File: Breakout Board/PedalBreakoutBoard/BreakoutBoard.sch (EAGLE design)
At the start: 40 parts, among them U1 ES_DAISY_SEED_REV4

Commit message: DP-16 - Update schematic to add new sheet
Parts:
- added J1: POWER_JACK, SparkFun-Connectors:POWER_JACK
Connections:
- new net 9V_IN: U1.V_IN
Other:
- note added: "?????"

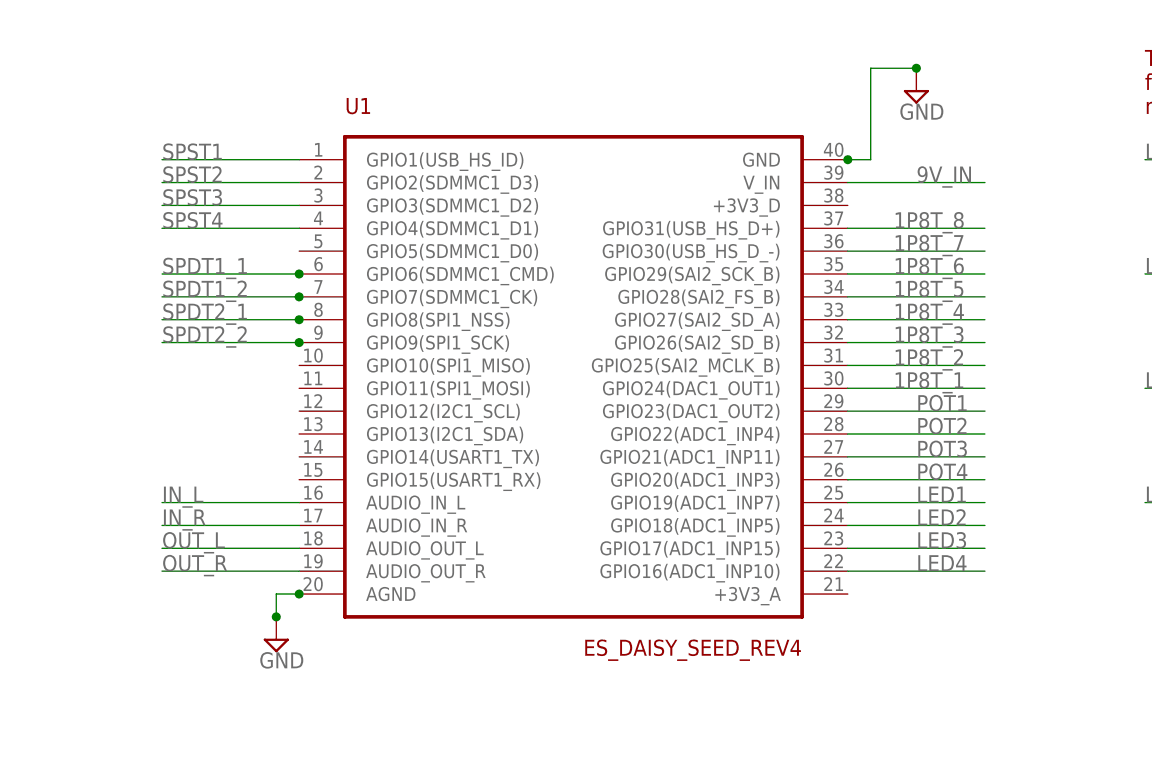
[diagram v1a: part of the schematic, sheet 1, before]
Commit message: DP-16 - Update schematic with correct 3V3 feeds
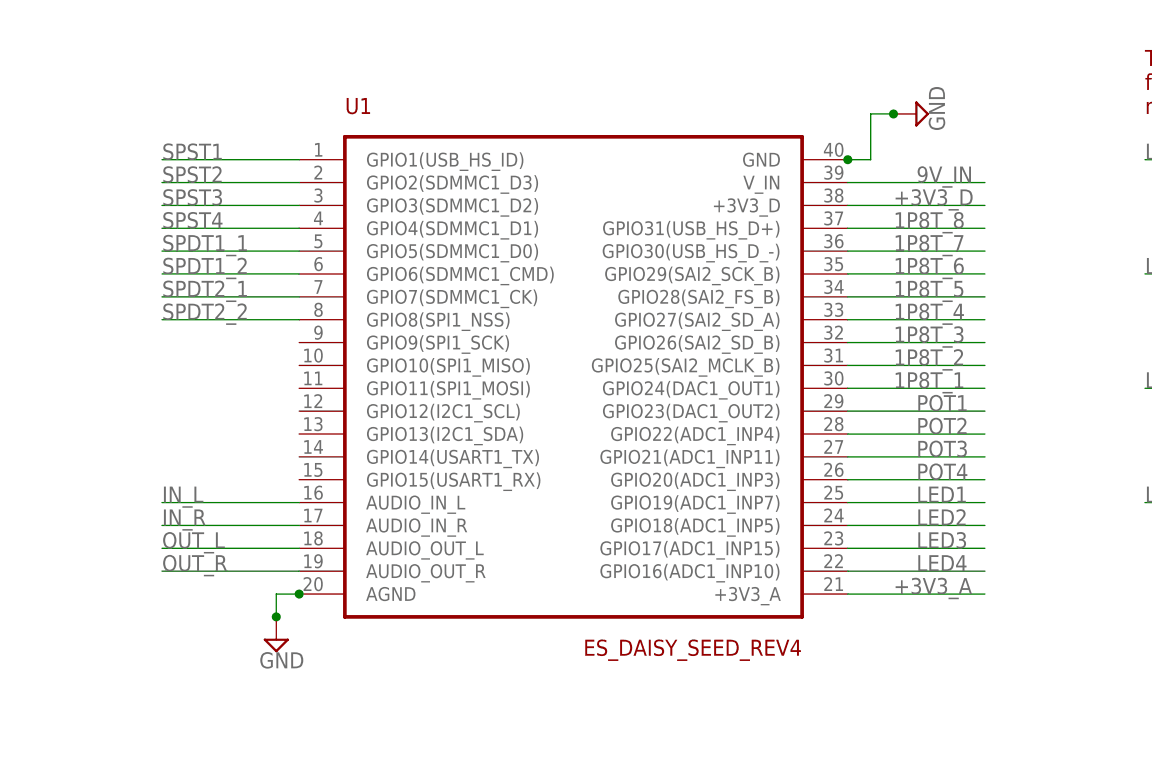
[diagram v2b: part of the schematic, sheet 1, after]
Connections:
- removed net +3V3: 1P8T.9, POT1.1, POT2.1, POT3.1, POT4.1, SPDT1.2, SPDT2.2, SPST1.1, SPST2.1, SPST3.1, SPST4.1
- new net +3V3_A: 1P8T.9, POT1.1, POT2.1, POT3.1, POT4.1, SPDT1.2, SPDT2.2, SPST1.1, SPST2.1, SPST3.1, SPST4.1, U1.+3V3_A
- new net +3V3_D: U1.+3V3_D
- net SPDT1_1: now also U1.GPIO5(SDMMC1_D0); no longer U1.GPIO6(SDMMC1_CMD)
- net SPDT1_2: now also U1.GPIO6(SDMMC1_CMD); no longer U1.GPIO7(SDMMC1_CK)
- net SPDT2_1: now also U1.GPIO7(SDMMC1_CK); no longer U1.GPIO8(SPI1_NSS)
- net SPDT2_2: now also U1.GPIO8(SPI1_NSS); no longer U1.GPIO9(SPI1_SCK)

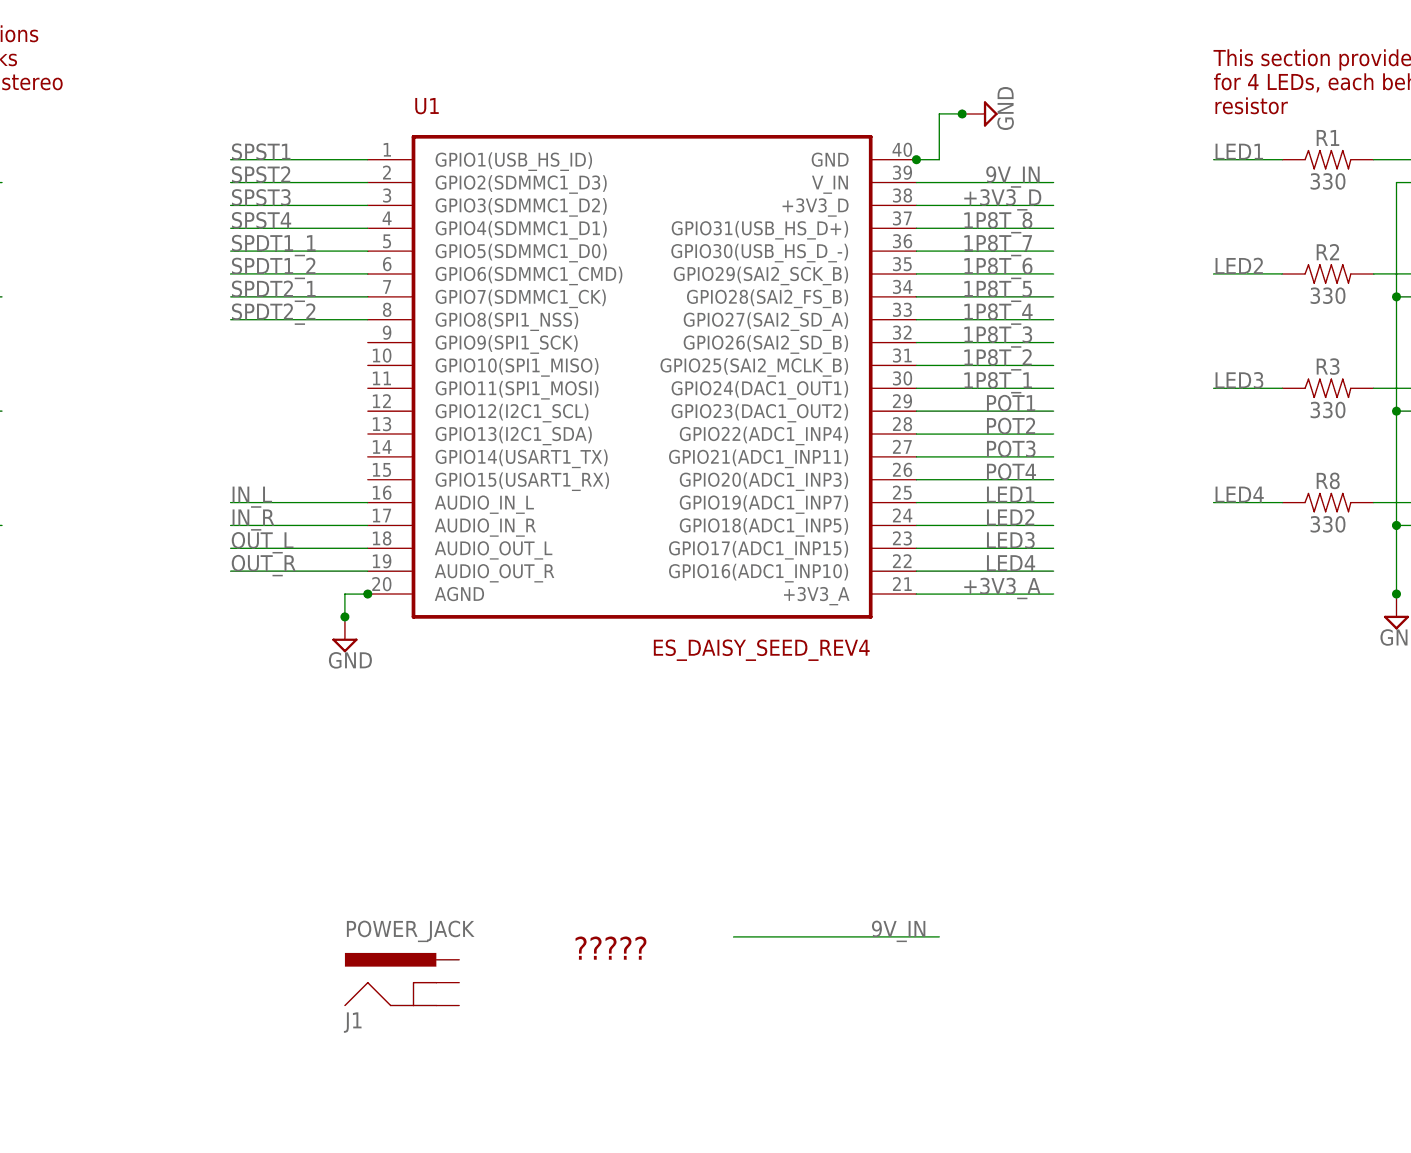
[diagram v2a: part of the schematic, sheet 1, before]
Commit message: DP-16 - Add power section
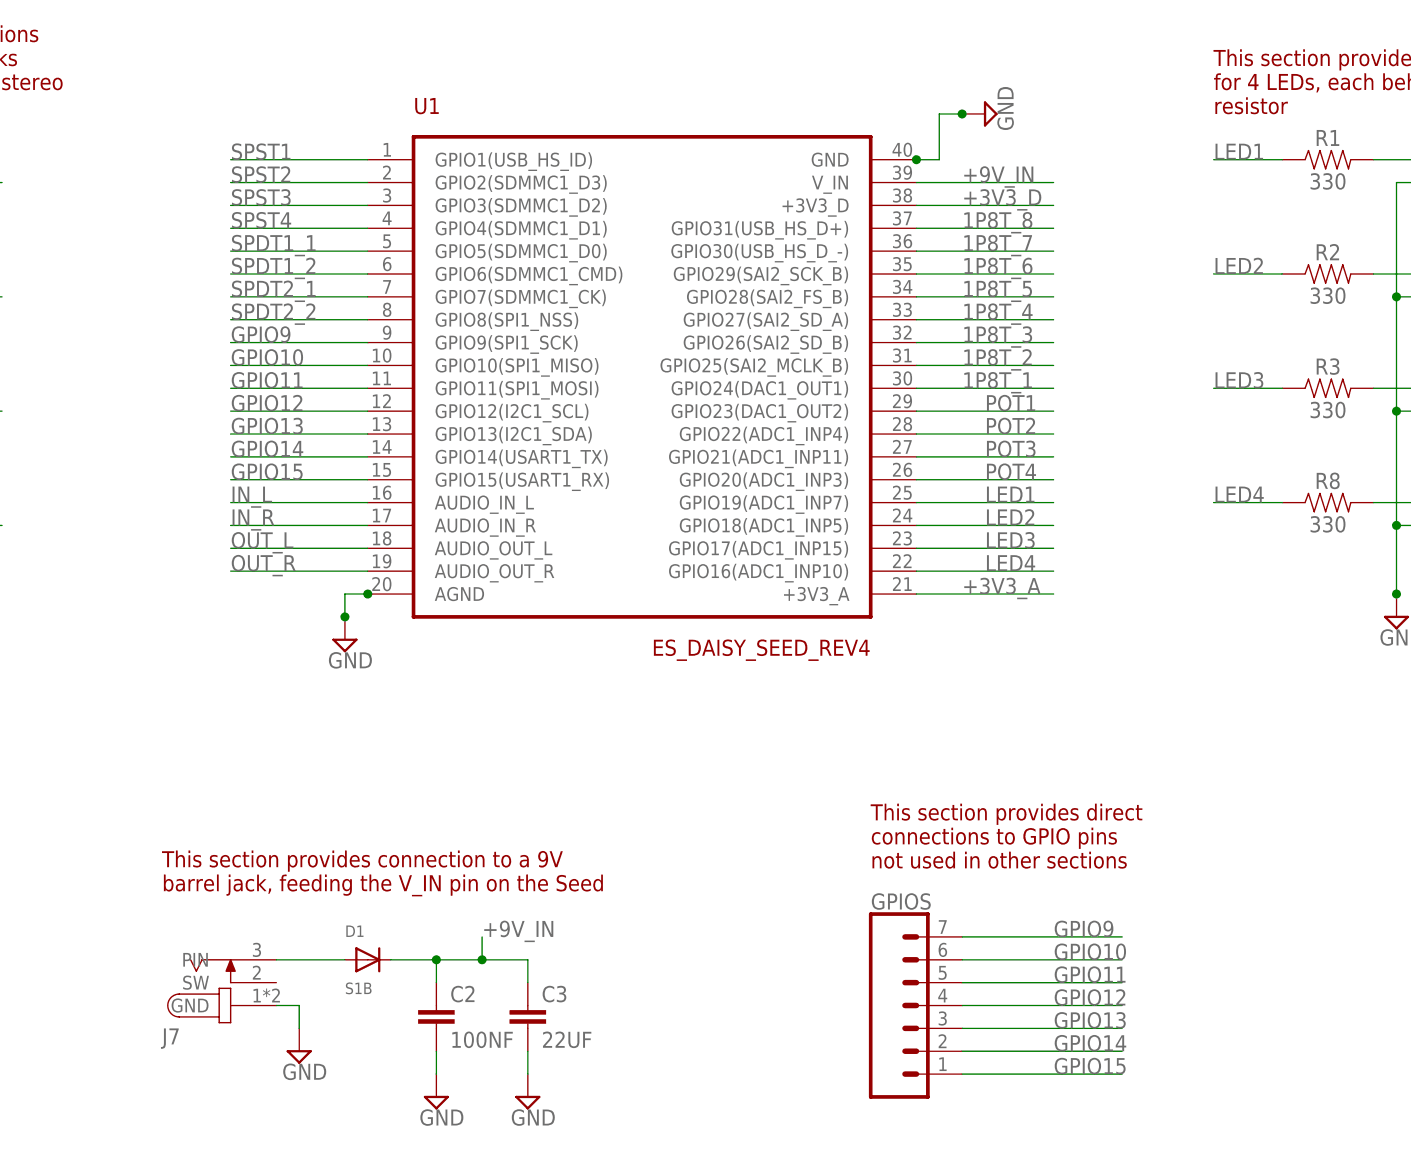
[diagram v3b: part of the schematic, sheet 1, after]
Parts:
- removed J1: POWER_JACK, SparkFun-Connectors:POWER_JACK
- added C2: 100NF, Electrosmith-Passives:C-EUC0603
- added C3: 22UF, Electrosmith-Passives:C-EUC1206
- added D1: S1B, Electrosmith-Semiconductors:S1B
- added GPIOS: (no value), SparkFun-Connectors:CONN_07
- added J7: SMT GUITAR DC JACK, Electrosmith-Connectors:GUITAR_DC_JACK
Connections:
- removed net 9V_IN: U1.V_IN
- new net +9V_IN: C2.1, C3.1, D1.C, U1.V_IN
- new net GPIO10: GPIOS.6, U1.GPIO10(SPI1_MISO)
- new net GPIO11: GPIOS.5, U1.GPIO11(SPI1_MOSI)
- new net GPIO12: GPIOS.4, U1.GPIO12(I2C1_SCL)
- new net GPIO13: GPIOS.3, U1.GPIO13(I2C1_SDA)
- new net GPIO14: GPIOS.2, U1.GPIO14(USART1_TX)
- new net GPIO15: GPIOS.1, U1.GPIO15(USART1_RX)
- new net GPIO9: GPIOS.7, U1.GPIO9(SPI1_SCK)
- new net N$2: D1.A, J7.PIN
- net GND: now also C2.2, C3.2, J7.GND
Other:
- note added: "This section provides connection to a 9V barrel jack, feeding the V_IN pin on the Seed"
- note added: "This section provides direct connections to GPIO pins not used in other sections"
- note removed: "?????"
